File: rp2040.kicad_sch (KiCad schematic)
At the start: 8 parts, among them U1 RP2040, Y1 12 MHz

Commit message: Savepoint!
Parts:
- C1, C2, C3, C6: footprint (none) -> Capacitor_Tantalum_SMD:CP_EIA-1608-08_AVX-J_HandSolder
- C7, C8: footprint (none) -> Capacitor_SMD:C_0402_1005Metric_Pad0.74x0.62mm_HandSolder
- Y1: footprint (none) -> Crystal:Crystal_SMD_3225-4Pin_3.2x2.5mm_HandSoldering
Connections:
- net COL_1: now reaches U1.14 (GPIO11)
- net COL_1: now also U1.3 (GPIO1)
- net COL_2: now reaches U1.15 (GPIO12)
- net COL_2: now also U1.4 (GPIO2)
- net COL_3: now reaches U1.16 (GPIO13)
- net COL_3: now also U1.5 (GPIO3)
- net COL_4: now reaches U1.17 (GPIO14)
- net COL_4: now also U1.6 (GPIO4)
- net COL_5: now reaches U1.18 (GPIO15)
- net COL_5: now also U1.7 (GPIO5)
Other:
- moved on the sheet: C1, C2, C3, C6, C7, C8, U1, Y1

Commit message: Savepoint!
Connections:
- net COL_1: no longer U1.14 (GPIO11)
- net COL_2: no longer U1.15 (GPIO12)
- net COL_3: no longer U1.16 (GPIO13)
- net COL_4: no longer U1.17 (GPIO14)
- net COL_5: no longer U1.18 (GPIO15)
- new net ROW_1: U1.14 (GPIO11)
- new net ROW_2: U1.15 (GPIO12)
- new net ROW_3: U1.16 (GPIO13)
- new net ROW_4: U1.17 (GPIO14)
- new net ROW_5: U1.18 (GPIO15)
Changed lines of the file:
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@@
+		)
+	)
+	(global_label "ROW_3"
+		(shape input)
+		(at 105.41 99.06 0)
+		(fields_autoplaced yes)
+		(effects
+			(font
+				(size 1.27 1.27)
+			)
+			(justify left)
+		)
+		(property "Intersheetrefs" "${INTERSHEET_REFS}"
+			(at 114.6242 99.06 0)
+			(hide yes)
+			(show_name no)
+			(do_not_autoplace no)
+			(effects
+				(font
+					(size 1.27 1.27)
+				)
+				(justify left)
+			)
+		)
+	)
+	(global_label "QSPI_SD3"
+		(shape input)
+		(at 54.61 111.76 180)
+		(fields_autoplaced yes)
+		(effects
+			(font
+				(size 1.27 1.27)
+			)
+			(justify right)
+		)
+		(property "Intersheetrefs" "${INTERSHEET_REFS}"
+			(at 42.5534 111.76 0)
+			(hide yes)
+			(show_name no)
+			(do_not_autoplace no)
+			(effects
+				(font
+					(size 1.27 1.27)
+				)
+				(justify right)
+			)
+		)
+	)
+	(global_label "QSPI_SD2"
+		(shape input)
+		(at 54.61 109.22 180)
+		(fields_autoplaced yes)
+		(effects
+			(font
+				(size 1.27 1.27)
+			)
+			(justify right)
+		)
+		(property "Intersheetrefs" "${INTERSHEET_REFS}"
+			(at 42.5534 109.22 0)
+			(hide yes)
+			(show_name no)
+			(do_not_autoplace no)
+			(effects
+				(font
+					(size 1.27 1.27)
+				)
+				(justify right)
+			)
+		)
+	)
+	(global_label "COL_1"
+		(shape input)
+		(at 105.41 68.58 0)
+		(fields_autoplaced yes)
+		(effects
+			(font
+				(size 1.27 1.27)
+			)
+			(justify left)
+		)
+		(property "Intersheetrefs" "${INTERSHEET_REFS}"
+			(at 114.2009 68.58 0)
+			(hide yes)
+			(show_name no)
+			(do_not_autoplace no)
+			(effects
+				(font
+					(size 1.27 1.27)
+				)
+				(justify left)
+			)
+		)
+	)
+	(global_label "COL_2"
+		(shape input)
+		(at 105.41 71.12 0)
+		(fields_autoplaced yes)
+		(effects
+			(font
+				(size 1.27 1.27)
+			)
+			(justify left)
+		)
+		(property "Intersheetrefs" "${INTERSHEET_REFS}"
+			(at 114.2009 71.12 0)
+			(hide yes)
+			(show_name no)
+			(do_not_autoplace no)
+			(effects
+				(font
+					(size 1.27 1.27)
+				)
+				(justify left)
+			)
+		)
+	)
+	(global_label "ROW_5"
+		(shape input)
+		(at 105.41 104.14 0)
+		(fields_autoplaced yes)
+		(effects
+			(font
+				(size 1.27 1.27)
+			)
+			(justify left)
+		)
+		(property "Intersheetrefs" "${INTERSHEET_REFS}"
+			(at 114.6242 104.14 0)
+			(hide yes)
+			(show_name no)
+			(do_not_autoplace no)
+			(effects
+				(font
+					(size 1.27 1.27)
+				)
+				(justify left)
+			)
+		)
+	)
+	(global_label "COL_5"
+		(shape input)
+		(at 105.41 78.74 0)
+		(fields_autoplaced yes)
+		(effects
+			(font
+				(size 1.27 1.27)
+			)
+			(justify left)
+		)
+		(property "Intersheetrefs" "${INTERSHEET_REFS}"
+			(at 114.2009 78.74 0)
+			(hide yes)
+			(show_name no)
+			(do_not_autoplace no)
+			(effects
+				(font
+					(size 1.27 1.27)
+				)
+				(justify left)
+			)
+		)
+	)
+	(global_label "QSPI_SS"
+		(shape input)
+		(at 54.61 99.06 180)
+		(fields_autoplaced yes)
+		(effects
+			(font
+				(size 1.27 1.27)
+			)
+			(justify right)
+		)
+		(property "Intersheetrefs" "${INTERSHEET_REFS}"
+			(at 43.8234 99.06 0)
+			(hide yes)
+			(show_name no)
+			(do_not_autoplace no)
+			(effects
+				(font
+					(size 1.27 1.27)
+				)
+				(justify right)
+			)
 		)
 	)
 	(global_label "COL_3"
 		(shape input)
-		(at 105.41 99.06 0)
-		(fields_autoplaced yes)
-		(effects
-			(font
-				(size 1.27 1.27)
-			)
-			(justify left)
-		)
-		(property "Intersheetrefs" "${INTERSHEET_REFS}"
-			(at 114.2009 99.06 0)
-			(hide yes)
-			(show_name no)
-			(do_not_autoplace no)
-			(effects
-				(font
-					(size 1.27 1.27)
-				)
-				(justify left)
-			)
-		)
-	)
-	(global_label "QSPI_SD3"
-		(shape input)
-		(at 54.61 111.76 180)
-		(fields_autoplaced yes)
-		(effects
-			(font
-				(size 1.27 1.27)
-			)
-			(justify right)
-		)
-		(property "Intersheetrefs" "${INTERSHEET_REFS}"
-			(at 42.5534 111.76 0)
-			(hide yes)
-			(show_name no)
-			(do_not_autoplace no)
-			(effects
-				(font
-					(size 1.27 1.27)
-				)
-				(justify right)
-			)
-		)
-	)
-	(global_label "QSPI_SD2"
-		(shape input)
-		(at 54.61 109.22 180)
-		(fields_autoplaced yes)
-		(effects
-			(font
-				(size 1.27 1.27)
-			)
-			(justify right)
-		)
-		(property "Intersheetrefs" "${INTERSHEET_REFS}"
-			(at 42.5534 109.22 0)
-			(hide yes)
-			(show_name no)
-			(do_not_autoplace no)
-			(effects
-				(font
-					(size 1.27 1.27)
-				)
-				(justify right)
-			)
-		)
-	)
-	(global_label "COL_1"
-		(shape input)
-		(at 105.41 68.58 0)
-		(fields_autoplaced yes)
-		(effects
-			(font
-				(size 1.27 1.27)
-			)
-			(justify left)
-		)
-		(property "Intersheetrefs" "${INTERSHEET_REFS}"
-			(at 114.2009 68.58 0)
-			(hide yes)
-			(show_name no)
-			(do_not_autoplace no)
-			(effects
-				(font
-					(size 1.27 1.27)
-				)
-				(justify left)
-			)
-		)
-	)
-	(global_label "COL_2"
-		(shape input)
-		(at 105.41 71.12 0)
-		(fields_autoplaced yes)
-		(effects
-			(font
-				(size 1.27 1.27)
-			)
-			(justify left)
-		)
-		(property "Intersheetrefs" "${INTERSHEET_REFS}"
-			(at 114.2009 71.12 0)
-			(hide yes)
-			(show_name no)
-			(do_not_autoplace no)
-			(effects
-				(font
-					(size 1.27 1.27)
-				)
-				(justify left)
-			)
-		)
-	)
-	(global_label "COL_5"
-		(shape input)
-		(at 105.41 104.14 0)
-		(fields_autoplaced yes)
-		(effects
-			(font
-				(size 1.27 1.27)
-			)
-			(justify left)
-		)
-		(property "Intersheetrefs" "${INTERSHEET_REFS}"
-			(at 114.2009 104.14 0)
-			(hide yes)
-			(show_name no)
-			(do_not_autoplace no)
-			(effects
-				(font
-					(size 1.27 1.27)
-				)
-				(justify left)
-			)
-		)
-	)
-	(global_label "COL_5"
-		(shape input)
-		(at 105.41 78.74 0)
-		(fields_autoplaced yes)
-		(effects
-			(font
-				(size 1.27 1.27)
-			)
-			(justify left)
-		)
-		(property "Intersheetrefs" "${INTERSHEET_REFS}"
-			(at 114.2009 78.74 0)
-			(hide yes)
-			(show_name no)
-			(do_not_autoplace no)
-			(effects
-				(font
-					(size 1.27 1.27)
-				)
-				(justify left)
-			)
-		)
-	)
-	(global_label "QSPI_SS"
-		(shape input)
-		(at 54.61 99.06 180)
-		(fields_autoplaced yes)
-		(effects
-			(font
-				(size 1.27 1.27)
-			)
-			(justify right)
-		)
-		(property "Intersheetrefs" "${INTERSHEET_REFS}"
-			(at 43.8234 99.06 0)
-			(hide yes)
-			(show_name no)
-			(do_not_autoplace no)
-			(effects
-				(font
-					(size 1.27 1.27)
-				)
-				(justify right)
-			)
-		)
-	)
-	(global_label "COL_3"
-		(shape input)
 		(at 105.41 73.66 0)
 		(fields_autoplaced yes)
@@
 		)
 	)
-	(global_label "COL_4"
+	(global_label "ROW_4"
 		(shape input)
 		(at 105.41 101.6 0)
@@
 		)
 		(property "Intersheetrefs" "${INTERSHEET_REFS}"
-			(at 114.2009 101.6 0)
-			(hide yes)
-			(show_name no)
-			(do_not_autoplace no)
-			(effects
-				(font
-					(size 1.27 1.27)
-				)
-				(justify left)
-			)
-		)
-	)
-	(global_label "COL_2"
+			(at 114.6242 101.6 0)
+			(hide yes)
+			(show_name no)
+			(do_not_autoplace no)
+			(effects
+				(font
+					(size 1.27 1.27)
+				)
+				(justify left)
+			)
+		)
+	)
+	(global_label "ROW_2"
 		(shape input)
 		(at 105.41 96.52 0)
@@
 		)
 		(property "Intersheetrefs" "${INTERSHEET_REFS}"
-			(at 114.2009 96.52 0)
+			(at 114.6242 96.52 0)
 			(hide yes)
 			(show_name no)
@@
 		)
 	)
-	(global_label "COL_1"
+	(global_label "ROW_1"
 		(shape input)
 		(at 105.41 93.98 0)
@@
 		)
 		(property "Intersheetrefs" "${INTERSHEET_REFS}"
-			(at 114.2009 93.98 0)
-			(hide yes)
-			(show_name no)
+			(at 114.6242 93.98 0)
+			(hide yes)
+			(show_name no)

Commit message: Savepoint!
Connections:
- net COL_1: now also U1.37 (GPIO25); no longer U1.3 (GPIO1)
- net COL_2: now also U1.36 (GPIO24); no longer U1.4 (GPIO2)
- net COL_3: now also U1.29 (GPIO18); no longer U1.5 (GPIO3)
- net COL_8: now reaches U1.11 (GPIO8)
- net COL_9: now reaches U1.12 (GPIO9)
- net COL_10: now reaches U1.13 (GPIO10)
- net COL_6: now reaches U1.8 (GPIO6)
- net COL_7: now reaches U1.9 (GPIO7)
- net ROW_3: no longer names the net of U1.16 (GPIO13)
- net ROW_4: no longer names the net of U1.17 (GPIO14)
- net ROW_5: no longer names the net of U1.18 (GPIO15)

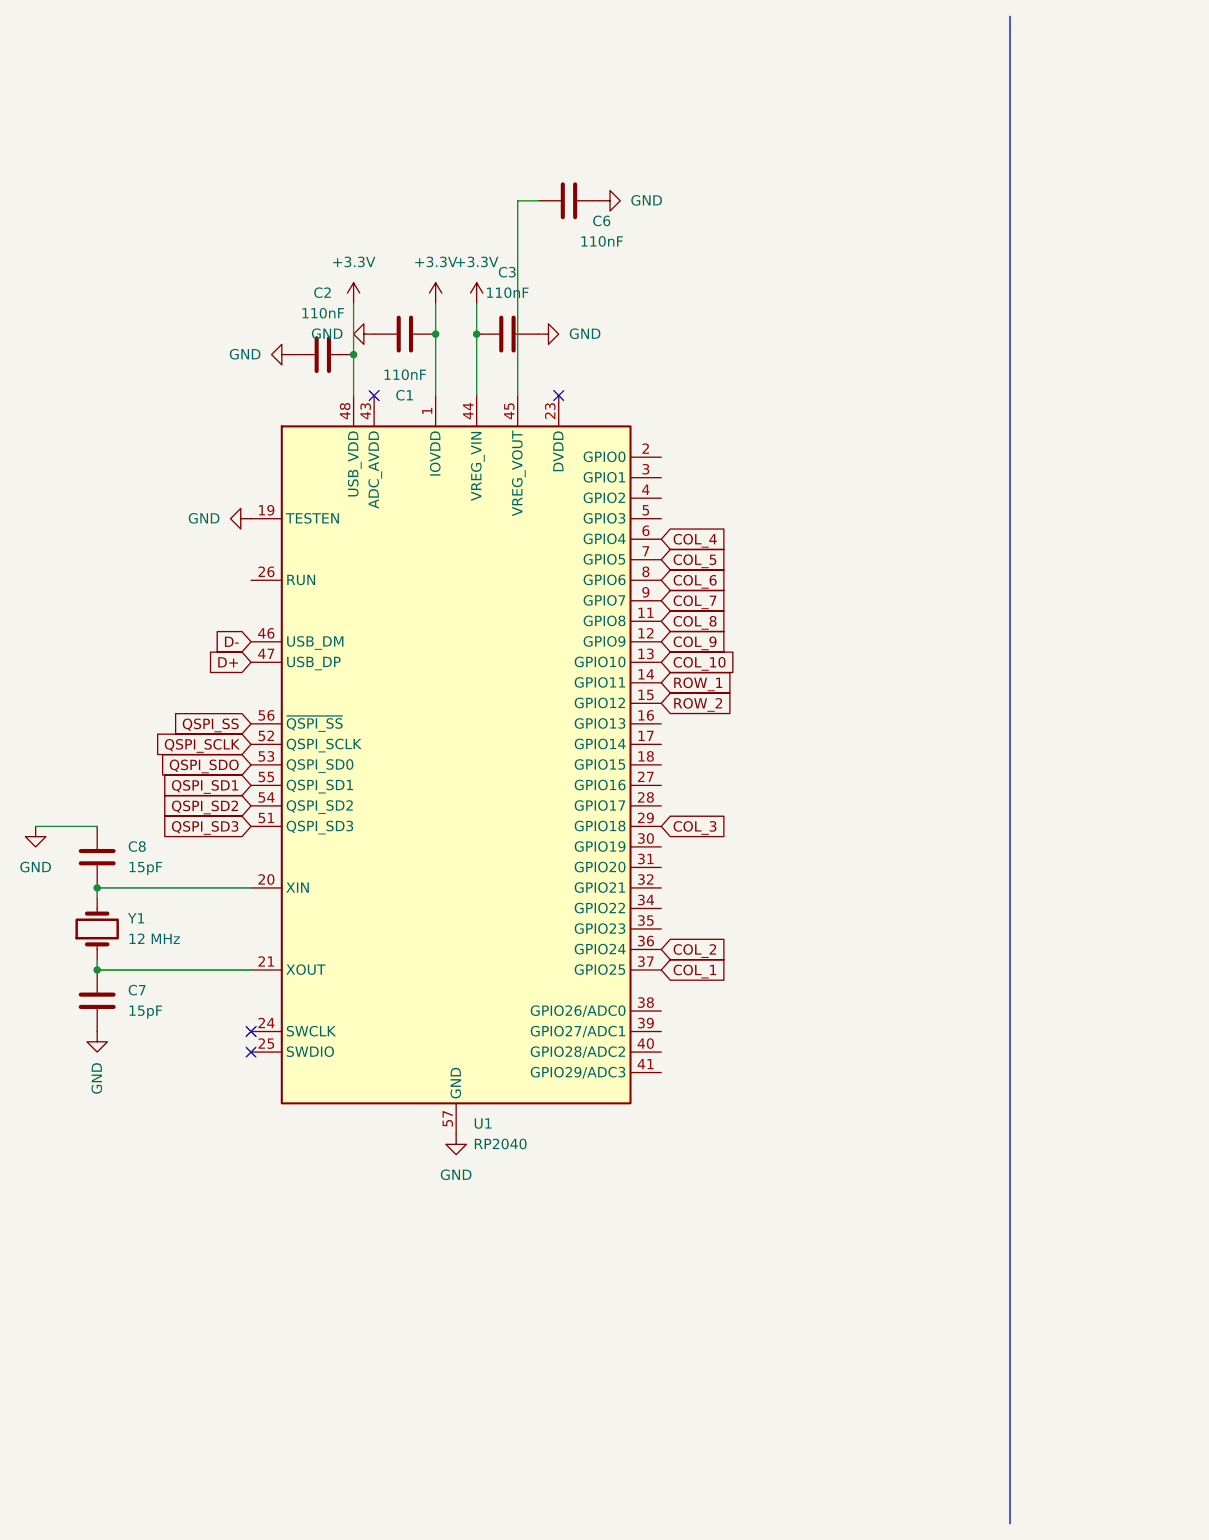
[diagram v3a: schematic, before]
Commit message: Smalled Caps and Restarting Layout.
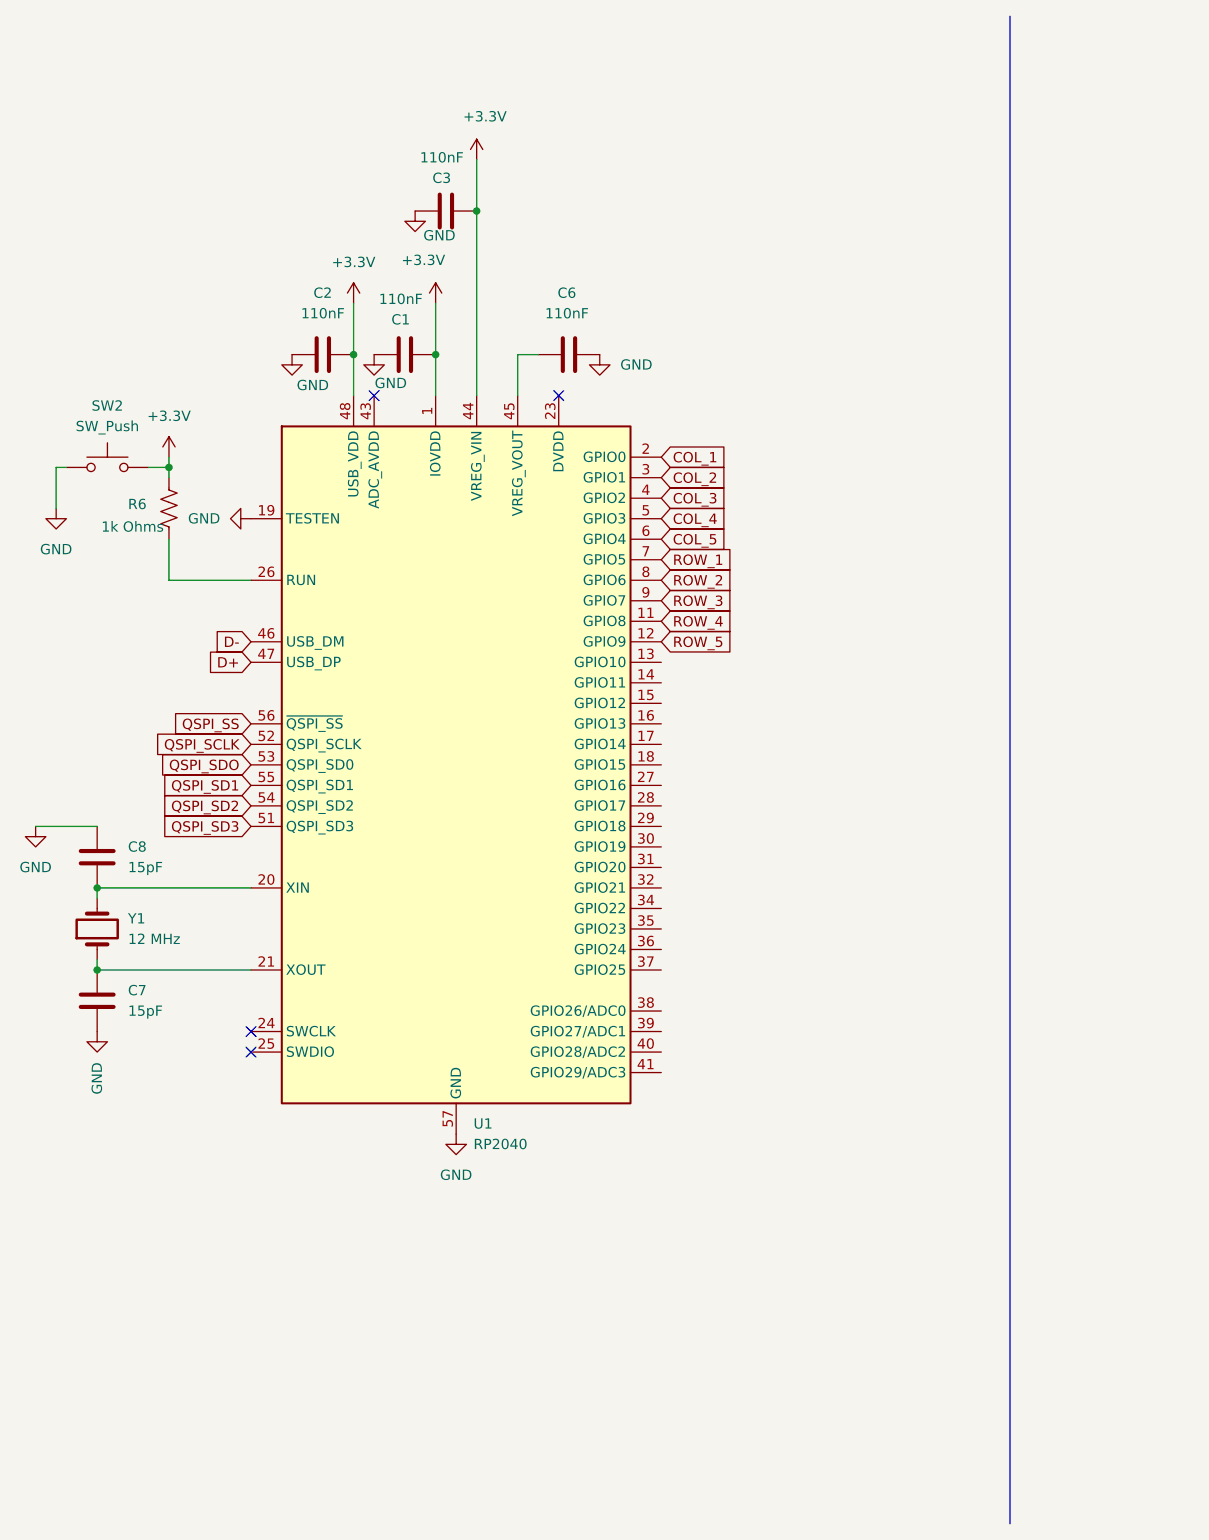
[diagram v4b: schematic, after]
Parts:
- added R6: 1k Ohms, Resistor_SMD:R_0402_1005Metric_Pad0.72x0.64mm_HandSolder, symbol Device:R_US
- added SW2: SW_Push, ScottoKeebs_Components:Button_MJTP1243, symbol Switch:SW_Push
- C1, C2, C3, C6: footprint Capacitor_Tantalum_SMD:CP_EIA-1608-08_AVX-J_HandSolder -> Capacitor_SMD:C_0402_1005Metric_Pad0.74x0.62mm_HandSolder
- Y1: footprint Crystal:Crystal_SMD_3225-4Pin_3.2x2.5mm_HandSoldering -> Crystal:Crystal_SMD_3215-2Pin_3.2x1.5mm
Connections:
- net COL_6 is gone; now on net ROW_2: U1.8 (GPIO6)
- net +3.3V: now also R6.1, SW2.2
- net COL_1: now also U1.2 (GPIO0); no longer U1.37 (GPIO25)
- net COL_2: now also U1.3 (GPIO1); no longer U1.36 (GPIO24)
- net COL_3: now also U1.4 (GPIO2); no longer U1.29 (GPIO18)
- net COL_4: now also U1.5 (GPIO3); no longer U1.6 (GPIO4)
- net COL_5: now also U1.6 (GPIO4); no longer U1.7 (GPIO5)
- net GND: now also SW2.1
- net ROW_1: now also U1.7 (GPIO5); no longer U1.14 (GPIO11)
- net ROW_2: no longer U1.15 (GPIO12)
- net at U1.26 (RUN): now also R6.2
- net COL_10: no longer names the net of U1.13 (GPIO10)
- net COL_7 renamed ROW_3
- net COL_8 renamed ROW_4
- net COL_9 renamed ROW_5
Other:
- moved on the sheet: C1, C3, C6

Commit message: Layout changes & wiring testing
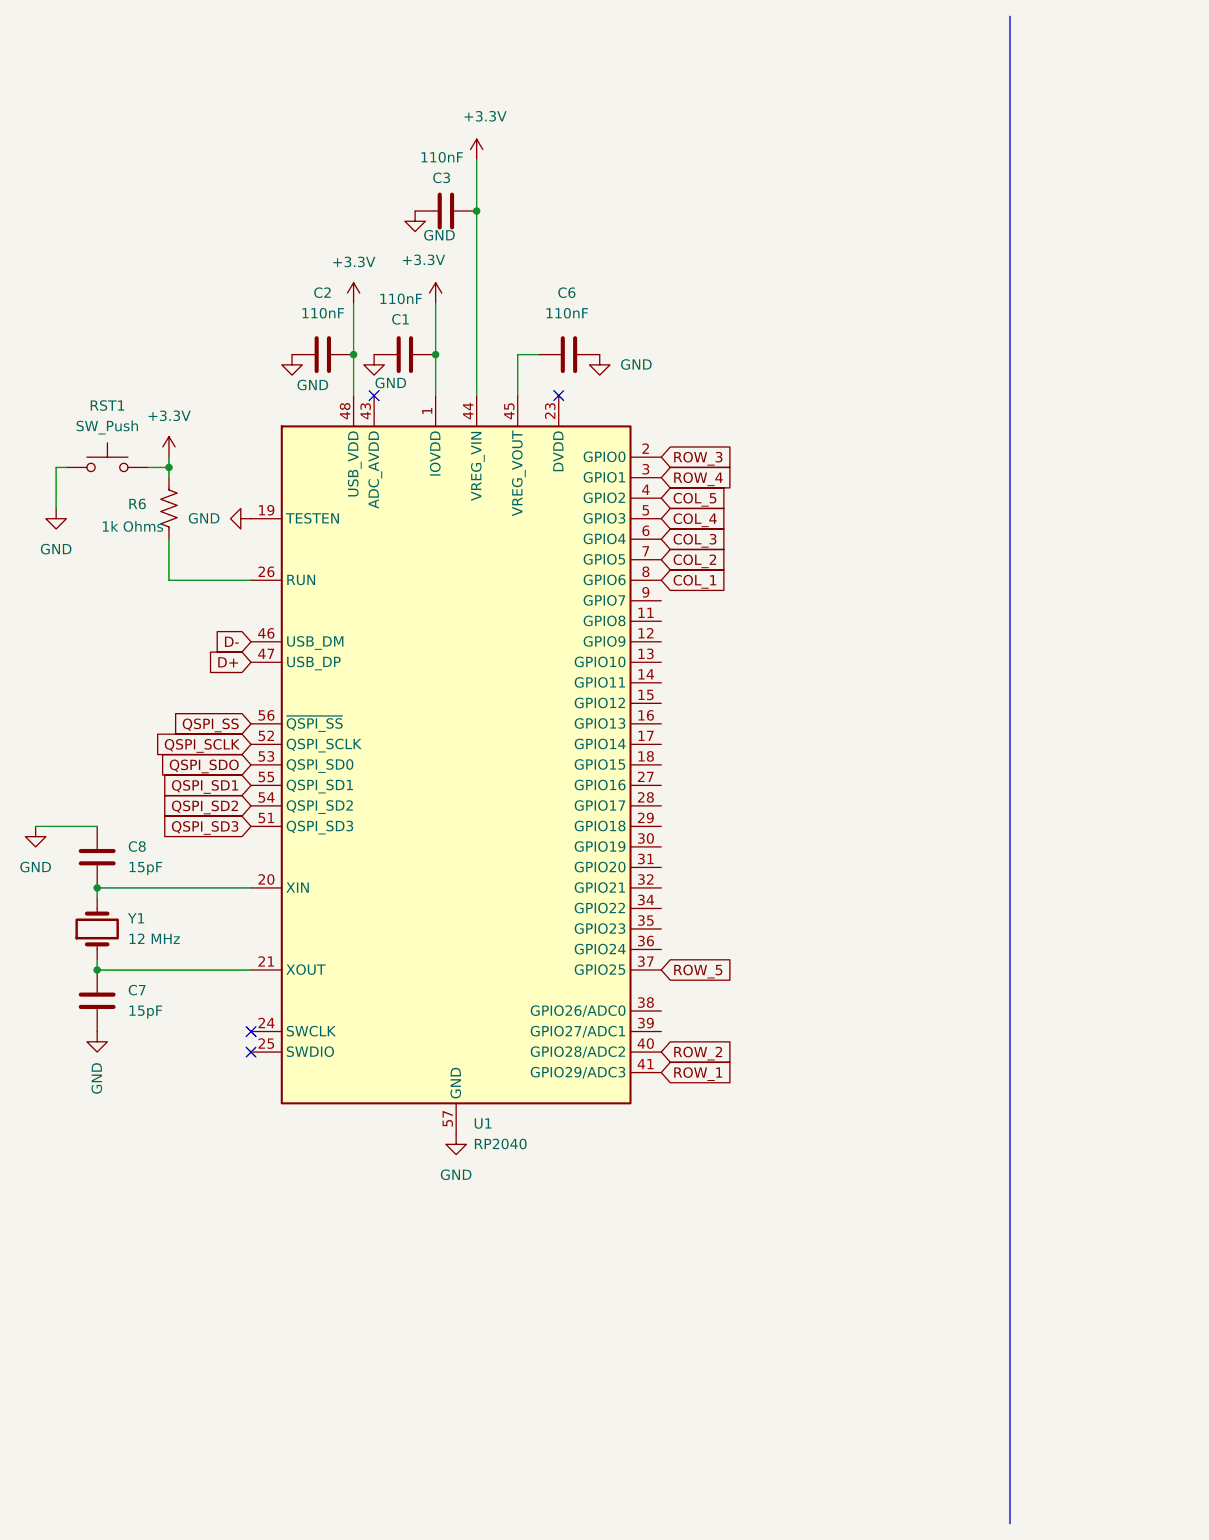
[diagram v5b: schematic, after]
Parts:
- renumbered SW2 to RST1
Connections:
- net COL_1: now also U1.8 (GPIO6); no longer U1.2 (GPIO0)
- net COL_2: now also U1.7 (GPIO5); no longer U1.3 (GPIO1)
- net COL_3: now also U1.6 (GPIO4); no longer U1.4 (GPIO2)
- net COL_5: now also U1.4 (GPIO2); no longer U1.6 (GPIO4)
- net ROW_1: now also U1.41 (GPIO29/ADC3); no longer U1.7 (GPIO5)
- net ROW_2: now also U1.40 (GPIO28/ADC2); no longer U1.8 (GPIO6)
- net ROW_3: now also U1.2 (GPIO0); no longer U1.9 (GPIO7)
- net ROW_4: now also U1.3 (GPIO1); no longer U1.11 (GPIO8)
- net ROW_5: now also U1.37 (GPIO25); no longer U1.12 (GPIO9)
